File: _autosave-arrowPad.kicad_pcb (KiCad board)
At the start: 2 copper layers, 59 x 61 mm, 22 parts, among them K1 KEYSW, K2 KEYSW, K3 KEYSW, K4 KEYSW, K5 KEYSW, K6 KEYSW, K7 KEYSW, K8 KEYSW, K9 KEYSW, SW1 SW_DIP_x01, U1 ProMicro, U2 NRF24L01_Breakout

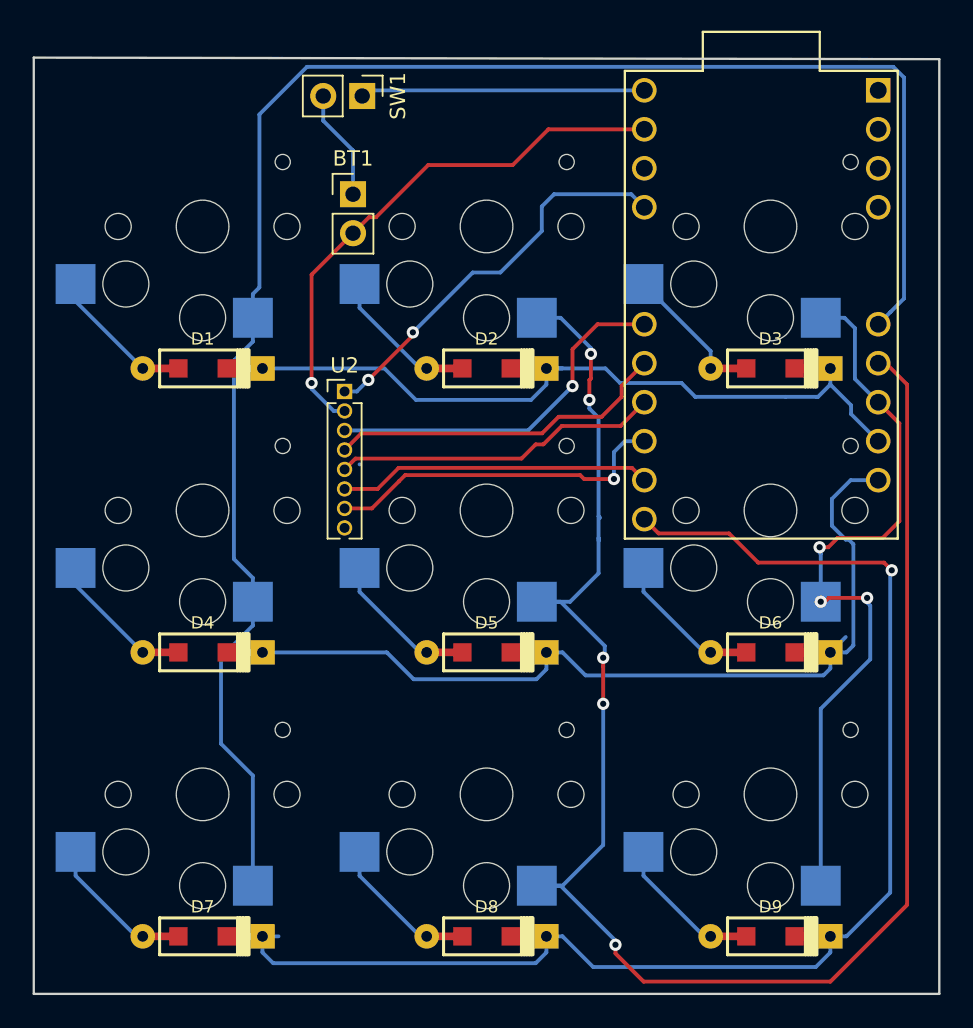
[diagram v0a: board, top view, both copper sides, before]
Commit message: added ground plane
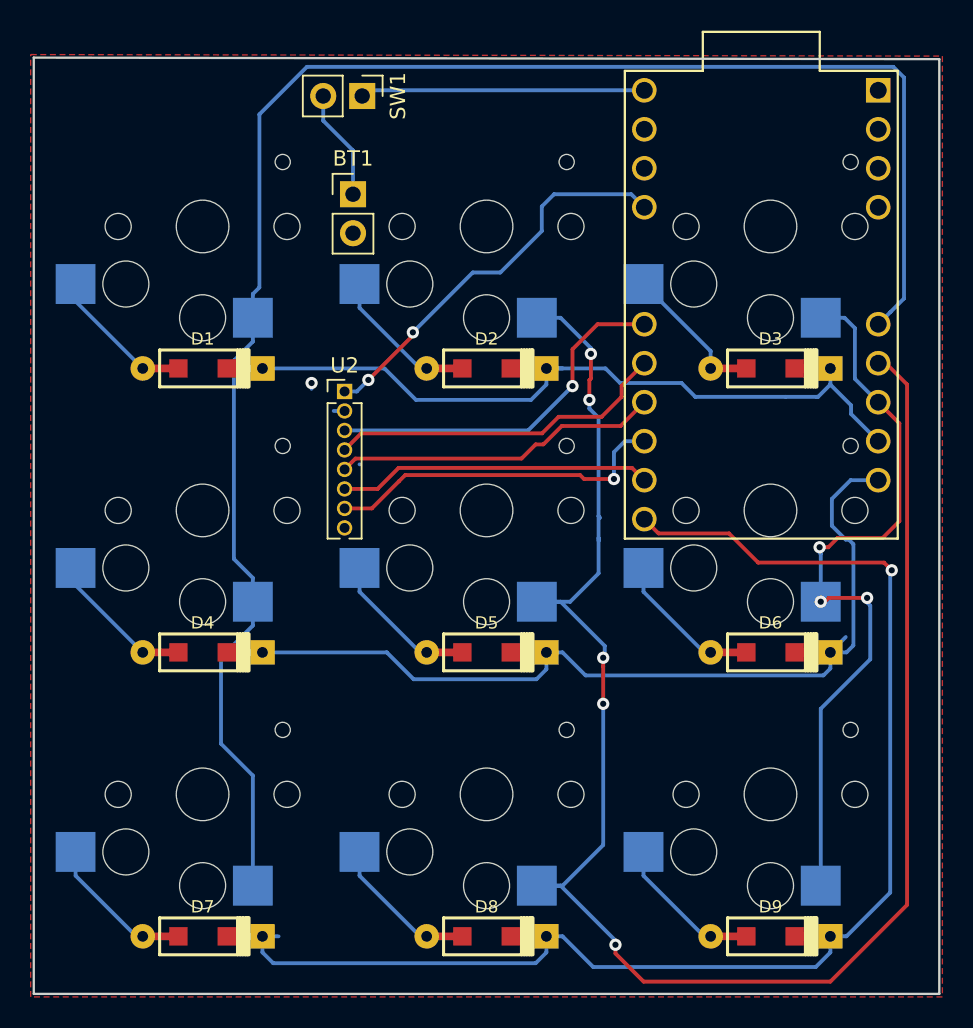
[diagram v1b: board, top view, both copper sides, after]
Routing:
- net /GND1: track 36.0 -> 1.33 mm
- added copper zone on F.Cu, net /GND1
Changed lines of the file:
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@@
     (thickness 1.6)
     (drawings 4)
-    (tracks 233)
+    (tracks 224)
     (zones 0)
     (modules 22)
@@
       (outputformat 1)
       (mirror false)
-      (drillshape 1)
+      (drillshape 0)
       (scaleselection 1)
       (outputdirectory ""))
@@
   (segment (start 80.78 83.63) (end 62.77 83.63) (width 0.25) (layer B.Cu) (net 1))
   (segment (start 61.25 104.52) (end 61.498462 104.52) (width 0.25) (layer F.Cu) (net 2))
-  (segment (start 60.542894 104.52) (end 59.1 103.077106) (width 0.25) (layer B.Cu) (net 2))
   (segment (start 61.25 104.52) (end 60.542894 104.52) (width 0.25) (layer B.Cu) (net 2))
   (via (at 59.1 102.7) (size 0.8) (drill 0.4) (layers F.Cu B.Cu) (net 2))
   (segment (start 59.1 103.077106) (end 59.1 102.7) (width 0.25) (layer B.Cu) (net 2))
-  (segment (start 59.1 95.64) (end 61.8 92.94) (width 0.25) (layer F.Cu) (net 2))
-  (segment (start 59.1 102.7) (end 59.1 95.64) (width 0.25) (layer F.Cu) (net 2))
-  (segment (start 61.8 92.94) (end 62.84 91.9) (width 0.25) (layer F.Cu) (net 2))
-  (segment (start 62.84 91.9) (end 63.3 91.9) (width 0.25) (layer F.Cu) (net 2))
-  (segment (start 63.3 91.9) (end 66.7 88.5) (width 0.25) (layer F.Cu) (net 2))
-  (segment (start 66.7 88.5) (end 72.2 88.5) (width 0.25) (layer F.Cu) (net 2))
-  (segment (start 74.53 86.17) (end 80.78 86.17) (width 0.25) (layer F.Cu) (net 2))
-  (segment (start 72.2 88.5) (end 74.53 86.17) (width 0.25) (layer F.Cu) (net 2))
   (segment (start 43.725 97.375) (end 43.725 96.25) (width 0.25) (layer B.Cu) (net 3))
   (segment (start 48.1 101.75) (end 43.725 97.375) (width 0.25) (layer B.Cu) (net 3))
@@
   (segment (start 61.8 87.55) (end 61.8 90.4) (width 0.25) (layer B.Cu) (net 30))
   (segment (start 59.86 85.61) (end 61.8 87.55) (width 0.25) (layer B.Cu) (net 30))
+  (zone (net 2) (net_name /GND1) (layer F.Cu) (hatch edge 0.508)
+    (connect_pads (clearance 0.254))
+    (min_thickness 0.254)
+    (fill yes (arc_segments 16) (thermal_gap 0.508) (thermal_bridge_width 0.508))
+    (polygon
+      (pts
+        (xy 100.2 81.4) (xy 100.2 142.7) (xy 40.8 142.7) (xy 40.8 81.3)
+      )
+    )
+  )
 )
